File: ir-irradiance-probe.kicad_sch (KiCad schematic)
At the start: 49 parts, among them J1 USB-C_UJC-HP-3-SMT-TR, J2 SM04B-SRSS-TB-LF-SN, J3 PinHeader_1x2_P2.54mm_Drill1.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, J4 Conn_BNC_031-70526-21, SW1 MSS3-V-T_R, U1 TLV70033_SC70, U2 AD8604ARUZ, U3 ADC101C027CIMK

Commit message: [#47284] Update potentiometer after standardisation
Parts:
- POT1: Author (none) -> Antmicro; License (none) -> Apache-2.0
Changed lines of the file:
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@@
       (effects (font (size 1.27 1.27)) hide)
+    )
+    (property "Author" "Antmicro" (id 6) (at 356.87 74.93 0)
+      (effects (font (size 1.27 1.27)) (justify left bottom) hide)
+    )
+    (property "License" "Apache-2.0" (id 7) (at 356.87 77.47 0)
+      (effects (font (size 1.27 1.27)) (justify left bottom) hide)
     )
     (pin "1")
@@
     (pin "2")
   )
-  (symbol (lib_id "antmicroRotaryPotentiometersRheostats:PTD902-1015K-B104") (at 336.55 121.92 0) (unit 2)
+  (symbol (lib_name "PTD902-1015K-B104_1") (lib_id "antmicroRotaryPotentiometersRheostats:PTD902-1015K-B104") (at 336.55 121.92 0) (unit 2)
     (in_bom yes) (on_board yes)
     (property "Reference" "POT1" (id 0) (at 339.09 115.57 0))
@@
       (effects (font (size 1.27 1.27)) hide)
     )
-    (pin "1")
+    (property "Author" "Antmicro" (id 6) (at 356.87 139.7 0)
+      (effects (font (size 1.27 1.27)) (justify left bottom) hide)
+    )
+    (property "License" "Apache-2.0" (id 7) (at 356.87 142.24 0)
+      (effects (font (size 1.27 1.27)) (justify left bottom) hide)
+    )
+    (pin "1")

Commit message: [#47284] Create local components library
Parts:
- C1, C2, C3, C4: footprint antmicro-footprints:C_0402_1005Metric -> ir-irradiance-probe-footprints:C_0402_1005Metric; symbol antmicroCapacitors0402:C_1u_0402 -> ir-irradiance-probe:C_1u_0402
- C10, C11: footprint antmicro-footprints:C_0402_1005Metric -> ir-irradiance-probe-footprints:C_0402_1005Metric; symbol antmicroCapacitors0402:C_180p_0402 -> ir-irradiance-probe:C_180p_0402
- C5, C7: footprint antmicro-footprints:C_0402_1005Metric -> ir-irradiance-probe-footprints:C_0402_1005Metric; symbol antmicroCapacitors0402:C_100n_0402 -> ir-irradiance-probe:C_100n_0402
- C6: footprint antmicro-footprints:C_0603_1608Metric -> ir-irradiance-probe-footprints:C_0603_1608Metric; symbol antmicroCapacitors0603:C_4u7_0603 -> ir-irradiance-probe:C_4u7_0603
- C8: footprint antmicro-footprints:C_0402_1005Metric -> ir-irradiance-probe-footprints:C_0402_1005Metric; symbol antmicroCapacitors0402:C_470p_0402 -> ir-irradiance-probe:C_470p_0402
- C9: footprint antmicro-footprints:C_0402_1005Metric -> ir-irradiance-probe-footprints:C_0402_1005Metric; symbol antmicroCapacitors0402:C_1n5_0402 -> ir-irradiance-probe:C_1n5_0402
- D1, D2, D3, D6: footprint antmicro-footprints:SOD-523 -> ir-irradiance-probe-footprints:SOD-523; symbol antmicroDiodesRectifiersSingle:RB521S30T1G -> ir-irradiance-probe:RB521S30T1G
- D4, D5: footprint antmicro-footprints:TPD2E009DRTR -> ir-irradiance-probe-footprints:TPD2E009DRTR; symbol antmicroTVSDiodes:PESD5V0S2BQA -> ir-irradiance-probe:PESD5V0S2BQA
- D7: footprint antmicro-footprints:LED_0603_1608Metric_G -> ir-irradiance-probe-footprints:LED_0603_1608Metric_G; symbol antmicroLEDIndicationDiscrete:LED_G_0603_LTST-C190GKT -> ir-irradiance-probe:LED_G_0603_LTST-C190GKT
- D8, D9: footprint antmicro-footprints:Photodiode_SMD_4.2x5mm_TEMD -> ir-irradiance-probe-footprints:Photodiode_SMD_4.2x5mm_TEMD; symbol antmicroOpticalSensorsReflectiveAnalogOutput:TEMD5020X01 -> ir-irradiance-probe:TEMD5020X01
- J1: footprint antmicro-footprints:USB-C_UJC-HP-3-SMT-TR -> ir-irradiance-probe-footprints:USB-C_UJC-HP-3-SMT-TR; symbol antmicroUSBDVIHDMIConnectors:USB-C_UJC-HP-3-SMT-TR -> ir-irradiance-probe:USB-C_UJC-HP-3-SMT-TR
- J2: footprint antmicro-footprints:SM04B-SRSS-TB-LF-SN -> ir-irradiance-probe-footprints:SM04B-SRSS-TB-LF-SN; symbol antmicroRectangularConnectorsHeadersMalePins:SM04B-SRSS-TB-LF-SN -> ir-irradiance-probe:SM04B-SRSS-TB-LF-SN
- J3: footprint antmicro-footprints:PinHeader_1x2_P2.54_Drill0.9mm -> ir-irradiance-probe-footprints:PinHeader_1x2_P2.54_Drill0.9mm; symbol antmicroRectangularConnectorsHeadersMalePins:PinHeader_1x2_P2.54mm_Drill1.1mm -> ir-irradiance-probe:PinHeader_1x2_P2.54mm_Drill1.1mm
- J4: footprint antmicro-footprints:Conn_BNC_031-70526-21 -> ir-irradiance-probe-footprints:Conn_BNC_031-70526-21; symbol antmicroCoaxialConnectorsRF:Conn_BNC_031-70526-21 -> ir-irradiance-probe:Conn_BNC_031-70526-21
- L1: footprint antmicro-footprints:L_0603_1608Metric -> ir-irradiance-probe-footprints:L_0603_1608Metric; symbol antmicroFixedInductors:L_2u2_0.2A_0603 -> ir-irradiance-probe:L_2u2_0.2A_0603
- MP1, MP2, MP3, MP4: footprint antmicro-footprints:mounting-hole-2.75mm-M2.5_D6.2mm_PTH -> ir-irradiance-probe-footprints:mounting-hole-2.75mm-M2.5_D6.2mm_PTH; symbol antmicroMechanicalParts:PCB_Mount_Hole_2.5_6.2 -> ir-irradiance-probe:PCB_Mount_Hole_2.5_6.2
- N1: footprint antmicro-footprints:antmicro-logo_scaled_20mm -> ir-irradiance-probe-footprints:antmicro-logo_scaled_20mm; symbol antmicroMechanicalParts:antmicro_logo -> ir-irradiance-probe:antmicro_logo
- N2: footprint antmicro-footprints:oshw-logo -> ir-irradiance-probe-footprints:oshw-logo; symbol antmicroMechanicalParts:oshw_logo -> ir-irradiance-probe:oshw_logo
- POT1: footprint antmicro-footprints:PTD902-1015K-B104 -> ir-irradiance-probe-footprints:PTD902-1015K-B104; symbol antmicroRotaryPotentiometersRheostats:PTD902-1015K-B104 -> ir-irradiance-probe:PTD902-1015K-B104
- R1, R2, R6, R7: footprint antmicro-footprints:R_0402_1005Metric -> ir-irradiance-probe-footprints:R_0402_1005Metric; symbol antmicroResistors0402:R_5k1_0402 -> ir-irradiance-probe:R_5k1_0402
- R10, R12: footprint antmicro-footprints:R_0402_1005Metric -> ir-irradiance-probe-footprints:R_0402_1005Metric; symbol antmicroResistors0402:R_47k_0402 -> ir-irradiance-probe:R_47k_0402
- R11, R9: footprint antmicro-footprints:R_0402_1005Metric -> ir-irradiance-probe-footprints:R_0402_1005Metric; symbol antmicroResistors0402:R_10k_0402 -> ir-irradiance-probe:R_10k_0402
- R13, R5: footprint antmicro-footprints:R_0402_1005Metric -> ir-irradiance-probe-footprints:R_0402_1005Metric; symbol antmicroResistors0402:R_0R_0402 -> ir-irradiance-probe:R_0R_0402
- R3: footprint antmicro-footprints:R_0402_1005Metric -> ir-irradiance-probe-footprints:R_0402_1005Metric; symbol antmicroResistors0402:R_1k2_0402 -> ir-irradiance-probe:R_1k2_0402
- R4: footprint antmicro-footprints:R_0402_1005Metric -> ir-irradiance-probe-footprints:R_0402_1005Metric; symbol antmicroResistors0402:R_22R_0402 -> ir-irradiance-probe:R_22R_0402
- R8: footprint antmicro-footprints:R_0402_1005Metric -> ir-irradiance-probe-footprints:R_0402_1005Metric; symbol antmicroResistors0402:R_1k_0402 -> ir-irradiance-probe:R_1k_0402
- SW1: footprint antmicro-footprints:Switch_Slide_MSS3 -> ir-irradiance-probe-footprints:Switch_Slide_MSS3; symbol antmicroSlideSwitches:MSS3-V-T_R -> ir-irradiance-probe:MSS3-V-T_R
- U1: footprint antmicro-footprints:SC-70-5 -> ir-irradiance-probe-footprints:SC-70-5; symbol antmicroPMICVoltageRegulatorsLinear:TLV70033_SC70 -> ir-irradiance-probe:TLV70033_SC70
- U2: footprint antmicro-footprints:TSSOP-14_4.4x5mm_P0.65mm -> ir-irradiance-probe-footprints:TSSOP-14_4.4x5mm_P0.65mm; symbol antmicroOperationalAmplifiers:AD8604ARUZ -> ir-irradiance-probe:AD8604ARUZ
- U3: footprint antmicro-footprints:SOT-23-6 -> ir-irradiance-probe-footprints:SOT-23-6; symbol antmicroDataAcquisitionAnalogtoDigitalConvertersADC:ADC101C027CIMK -> ir-irradiance-probe:ADC101C027CIMK

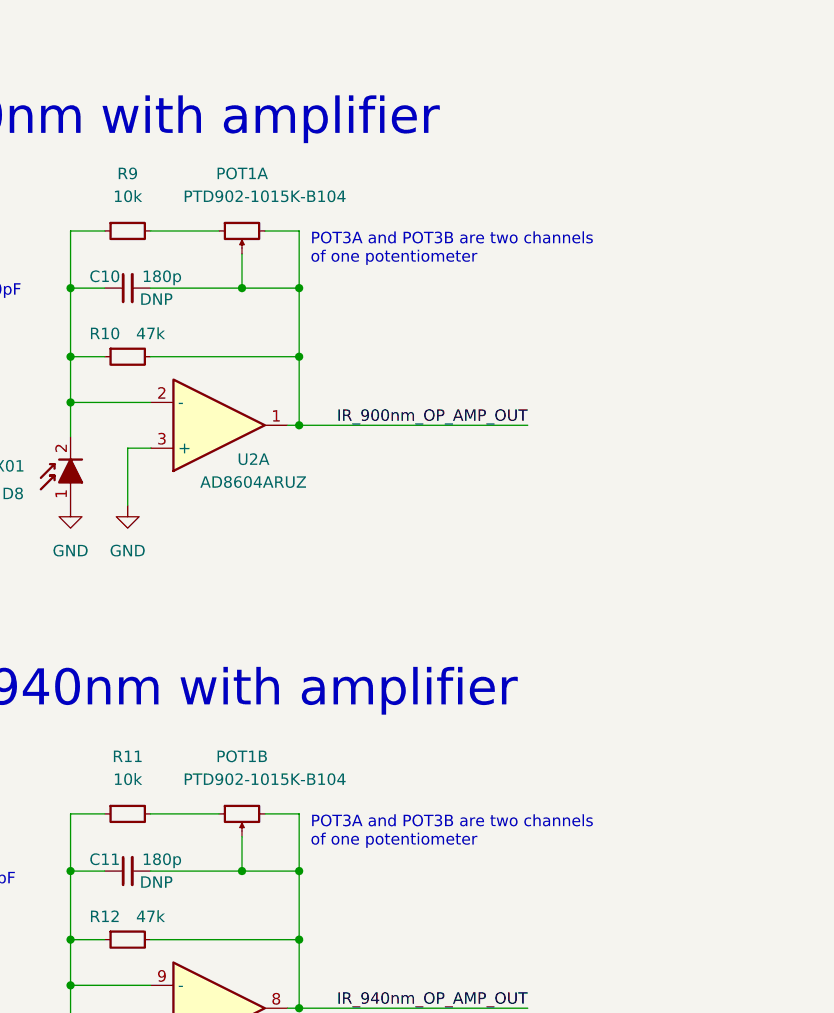
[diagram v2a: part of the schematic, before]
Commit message: [#47284] Change potentiometers on schematic
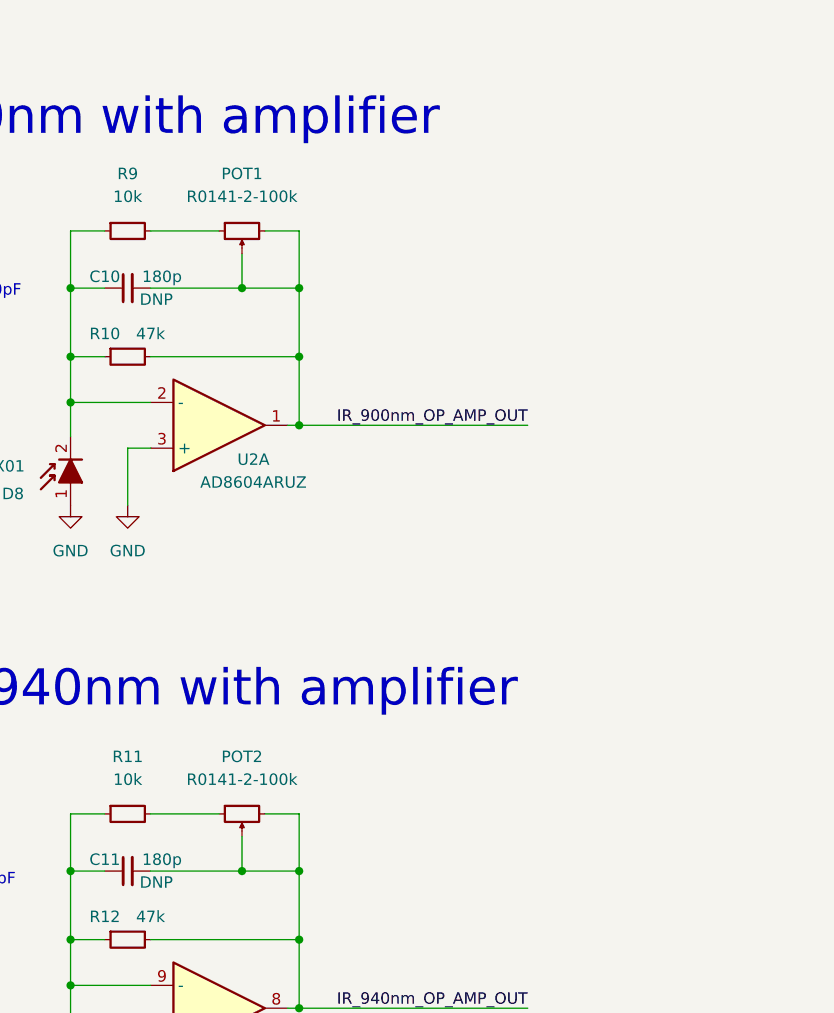
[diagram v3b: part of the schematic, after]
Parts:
- removed POT1: PTD902-1015K-B104, ir-irradiance-probe-footprints:PTD902-1015K-B104, symbol ir-irradiance-probe:PTD902-1015K-B104
- added POT1, POT2: POT_100k_R0141-2-100k, antmicro-footprints:POT_R0141-2, symbol antmicroRotaryPotentiometersRheostats:POT_100k_R0141-2-100k
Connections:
- net IR_900nm_OP_AMP_OUT: now also POT1.2, POT1.3
- net IR_940nm_OP_AMP_OUT: now also POT2.2, POT2.3
- net at R9.2: now also POT1.1
- net at R11.2: now also POT2.1
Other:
- note removed: "POT3A and POT3B are two channels of one potentiometer"

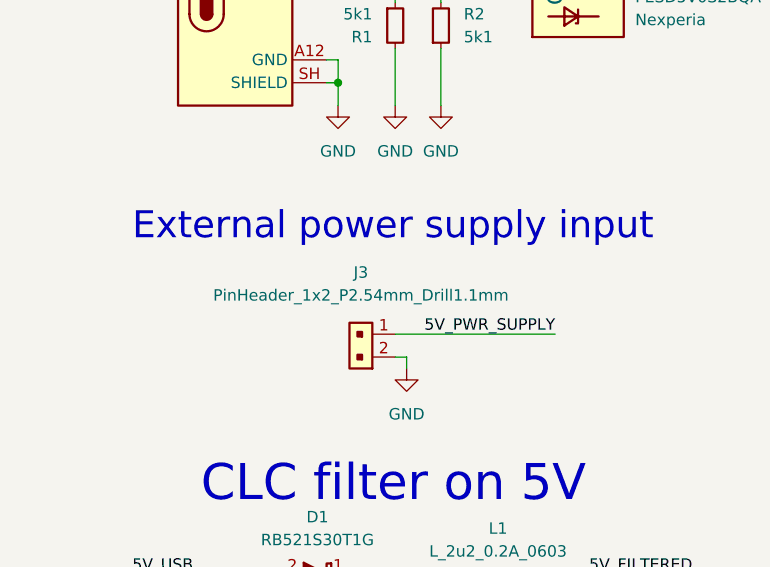
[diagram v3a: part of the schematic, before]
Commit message: [#47284] Change pin header to horizontal
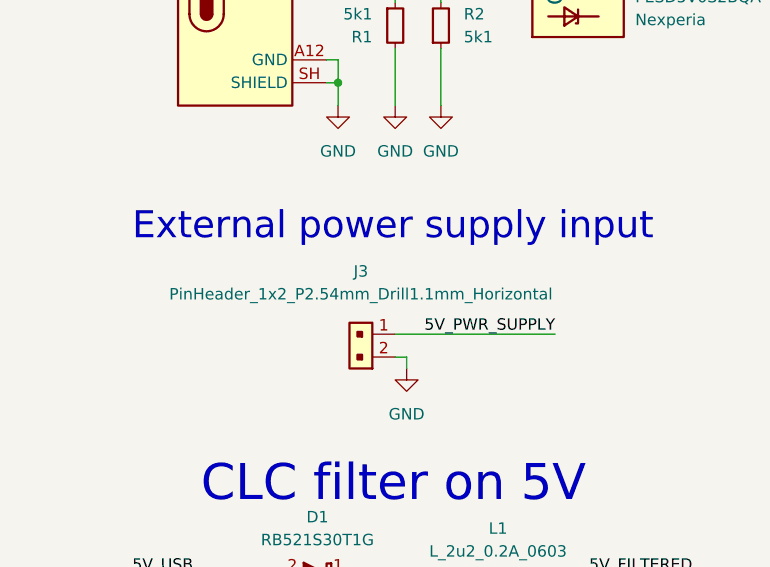
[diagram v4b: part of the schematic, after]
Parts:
- removed J3: PinHeader_1x2_P2.54mm_Drill1.1mm, ir-irradiance-probe-footprints:PinHeader_1x2_P2.54_Drill0.9mm, symbol ir-irradiance-probe:PinHeader_1x2_P2.54mm_Drill1.1mm
- added J3: PinHeader_1x2_P2.54mm_Drill1.1mm_Horizontal, ir-irradiance-probe-footprints:PinHeader_1x02_P2.54mm_Horizontal, symbol ir-irradiance-probe:PinHeader_1x2_P2.54mm_Drill1.1mm_Horizontal
- POT1, POT2: footprint antmicro-footprints:POT_R0141-2 -> ir-irradiance-probe-footprints:POT_R0141-2; symbol antmicroRotaryPotentiometersRheostats:POT_100k_R0141-2-100k -> ir-irradiance-probe:POT_100k_R0141-2-100k
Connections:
- net 5V_PWR_SUPPLY: now also J3.1
- net GND: now also J3.2

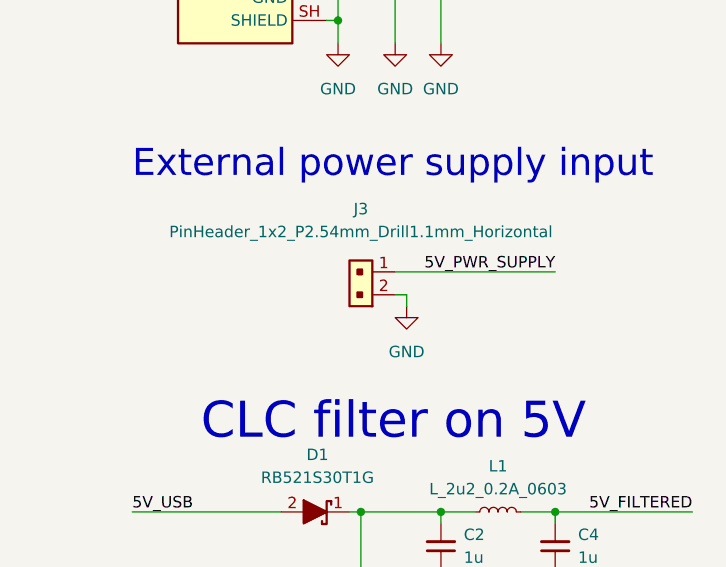
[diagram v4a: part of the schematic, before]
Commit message: [#47284] Mark J3 PinHeader as DNP
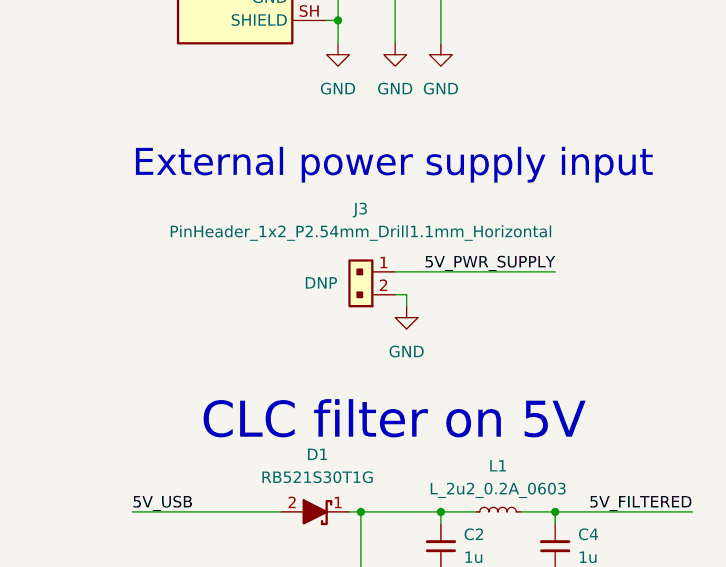
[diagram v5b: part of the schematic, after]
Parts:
- J3: DNP (none) -> DNP

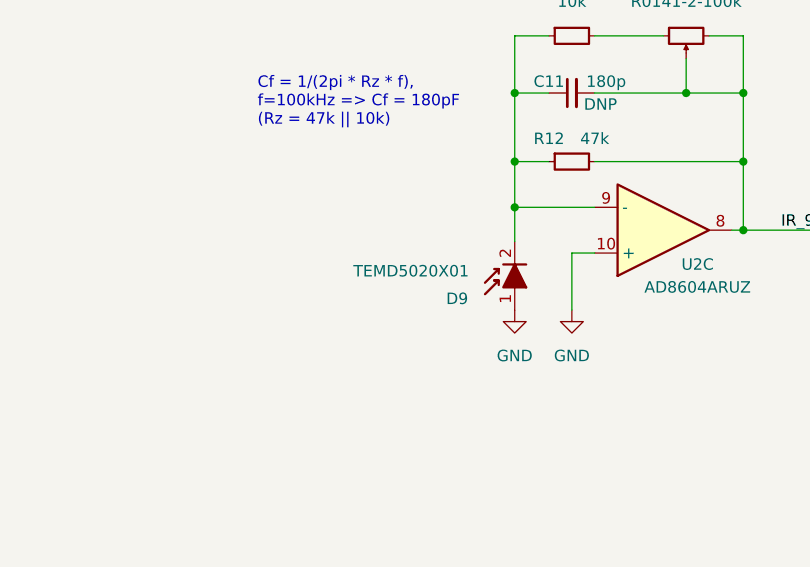
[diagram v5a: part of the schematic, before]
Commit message: [#47284] Change bottom photodiode from TEMD5020X01 to TEMD5110X01
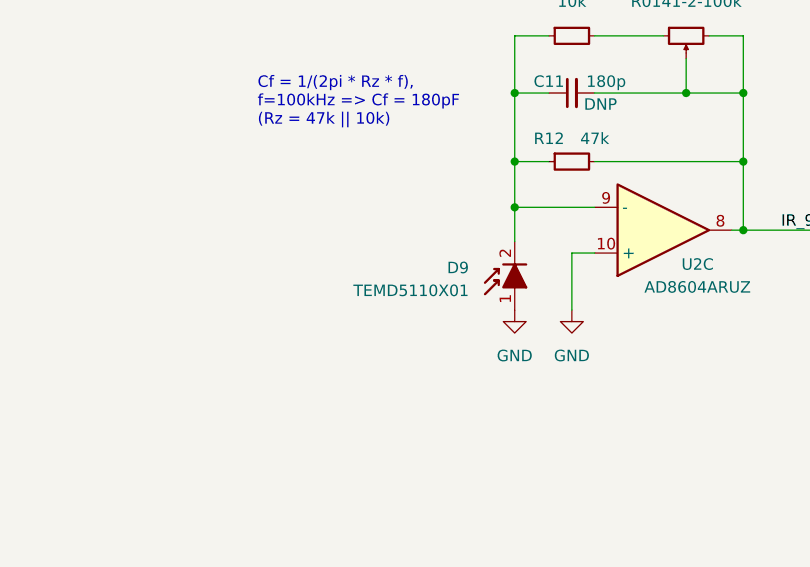
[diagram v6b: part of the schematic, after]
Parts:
- removed D9: TEMD5020X01, ir-irradiance-probe-footprints:Photodiode_SMD_4.2x5mm_TEMD, symbol ir-irradiance-probe:TEMD5020X01
- added D9: TEMD5110X01, antmicro-footprints:Photodiode_SMD_4.2x5mm_TEMD, symbol antmicroOpticalSensorsReflectiveAnalogOutput:TEMD5110X01
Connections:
- net GND: now also D9.1
- net at C11.1, R11.1, R12.1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: now also D9.2
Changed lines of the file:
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@@
     (pin "1")
-  )
-  (symbol (lib_id "ir-irradiance-probe:TEMD5020X01") (at 320.04 152.4 90) (unit 1)
-    (in_bom yes) (on_board yes)
-    (property "Reference" "D9" (id 0) (at 312.42 151.13 90)
-      (effects (font (size 1.27 1.27) (thickness 0.15)) (justify right))
-    )
-    (property "Value" "TEMD5020X01" (id 1) (at 314.96 147.32 90)
-      (effects (font (size 1.27 1.27) (thickness 0.15)) (justify left bottom))
-    )
-    (property "Footprint" "ir-irradiance-probe-footprints:Photodiode_SMD_4.2x5mm_TEMD" (id 2) (at 327.66 129.54 0)
-      (effects (font (size 1.27 1.27) (thickness 0.15)) (justify left bottom) hide)
-    )
-    (property "Datasheet" "https://4donline.ihs.com/images/VipMasterIC/IC/VISH/VISH-S-A0011530495/VISH-S-A0012000322-1.pdf?hkey=6D3A4C79FDBF58556ACFDE234799DDF0" (id 3) (at 330.2 129.54 0)
-      (effects (font (size 1.27 1.27) (thickness 0.15)) (justify left bottom) hide)
-    )
-    (property "MPN" "TEMD5020X01" (id 4) (at 332.74 129.54 0)
-      (effects (font (size 1.27 1.27) (thickness 0.15)) (justify left bottom) hide)
-    )
-    (property "Manufacturer" "VISHAY" (id 5) (at 335.28 129.54 0)
-      (effects (font (size 1.27 1.27) (thickness 0.15)) (justify left bottom) hide)
-    )
-    (property "Author" "Antmicro" (id 6) (at 337.82 129.54 0)
-      (effects (font (size 1.27 1.27) (thickness 0.15)) (justify left bottom) hide)
-    )
-    (property "License" "Apache-2.0" (id 7) (at 340.36 129.54 0)
-      (effects (font (size 1.27 1.27) (thickness 0.15)) (justify left bottom) hide)
-    )
-    (pin "1")
-    (pin "2")
   )
   (symbol (lib_id "ir-irradiance-probe:GND") (at 260.35 217.17 0) (unit 1)
@@
     (pin "3")
   )
+  (symbol (lib_id "antmicroOpticalSensorsReflectiveAnalogOutput:TEMD5110X01") (at 320.04 152.4 90) (unit 1)
+    (in_bom yes) (on_board yes) (fields_autoplaced)
+    (property "Reference" "D9" (id 0) (at 314.96 147.7009 90)
+      (effects (font (size 1.27 1.27) (thickness 0.15)) (justify left))
+    )
+    (property "Value" "TEMD5110X01" (id 1) (at 314.96 150.2409 90)
+      (effects (font (size 1.27 1.27) (thickness 0.15)) (justify left))
+    )
+    (property "Footprint" "antmicro-footprints:Photodiode_SMD_4.2x5mm_TEMD" (id 2) (at 327.66 128.27 0)
+      (effects (font (size 1.27 1.27) (thickness 0.15)) (justify left bottom) hide)
+    )
+    (property "Datasheet" "https://www.farnell.com/datasheets/2243598.pdf" (id 3) (at 330.2 128.27 0)
+      (effects (font (size 1.27 1.27) (thickness 0.15)) (justify left bottom) hide)
+    )
+    (property "MPN" "TEMD5110X01" (id 4) (at 332.74 128.27 0)
+      (effects (font (size 1.27 1.27) (thickness 0.15)) (justify left bottom) hide)
+    )
+    (property "Manufacturer" "VISHAY" (id 5) (at 335.28 128.27 0)
+      (effects (font (size 1.27 1.27) (thickness 0.15)) (justify left bottom) hide)
+    )
+    (property "Author" "Antmicro" (id 6) (at 337.82 128.27 0)
+      (effects (font (size 1.27 1.27) (thickness 0.15)) (justify left bottom) hide)
+    )
+    (property "License" "Apache-2.0" (id 7) (at 340.36 128.27 0)
+      (effects (font (size 1.27 1.27) (thickness 0.15)) (justify left bottom) hide)
+    )
+    (pin "1")
+    (pin "2")
+  )
   (symbol (lib_id "ir-irradiance-probe:RB521S30T1G") (at 40.64 134.62 0) (mirror x) (unit 1)
     (in_bom yes) (on_board yes) (fields_autoplaced)
@@
       (reference "D8") (unit 1) (value "TEMD5020X01") (footprint "ir-irradiance-probe-footprints:Photodiode_SMD_4.2x5mm_TEMD")
     )
-    (path "/11865aa2-358e-40ea-a37f-9dbe26ee5368"
-      (reference "D9") (unit 1) (value "TEMD5020X01") (footprint "ir-irradiance-probe-footprints:Photodiode_SMD_4.2x5mm_TEMD")
+    (path "/dbef05c0-6afb-42a2-88e0-c7d67109c18c"
+      (reference "D9") (unit 1) (value "TEMD5110X01") (footprint "antmicro-footprints:Photodiode_SMD_4.2x5mm_TEMD")
     )
     (path "/b7aef2d3-216a-42aa-a19f-639fbaee2c8e"
